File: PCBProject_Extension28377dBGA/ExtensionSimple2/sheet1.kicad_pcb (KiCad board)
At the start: 4 copper layers, 122.2 x 82.1 mm, 88 parts, among them J1 Conn_02x05_Odd_Even, J2 Conn_01x02_Pin, J3 Conn_01x02_Pin, Q1 FMMT618TA, U1 SN74ABT541, U2 SN74ABT541

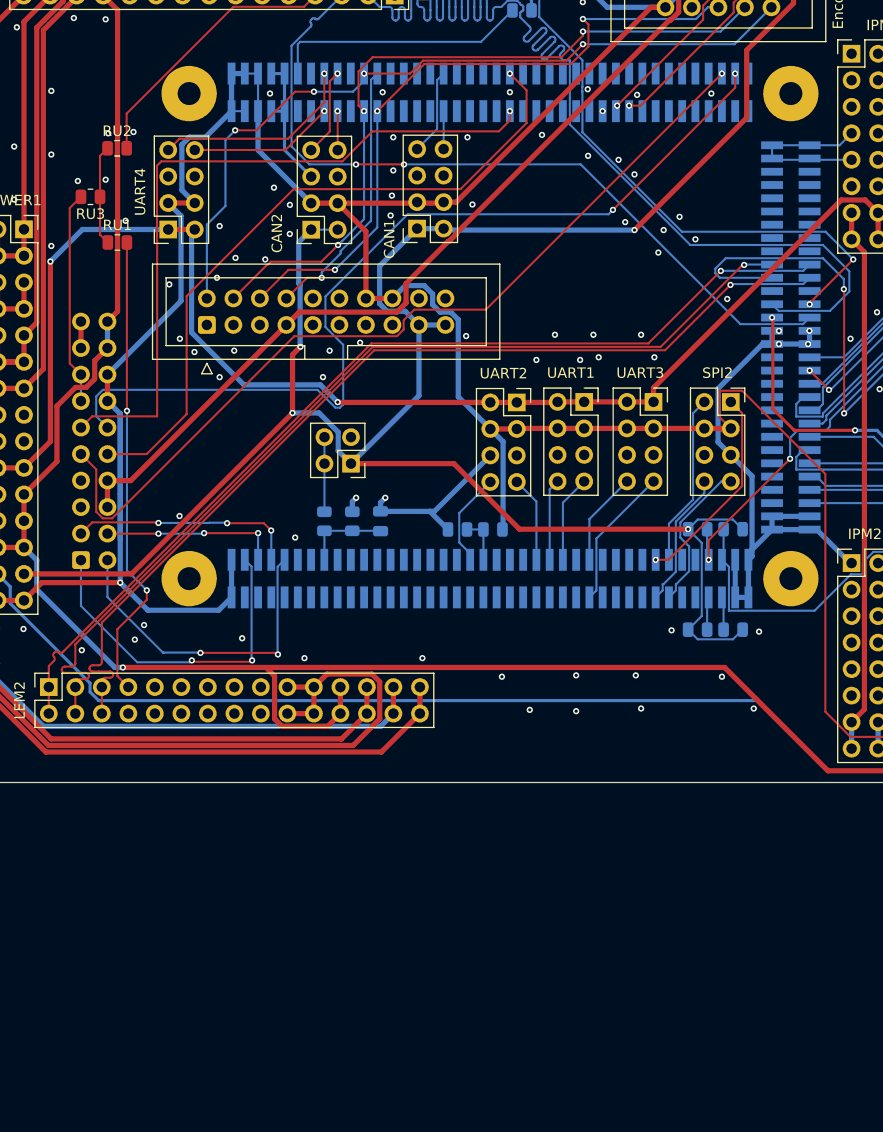
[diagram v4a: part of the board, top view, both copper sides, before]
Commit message: 底板原理图中加入RS485通讯芯片—-SN65HVD75
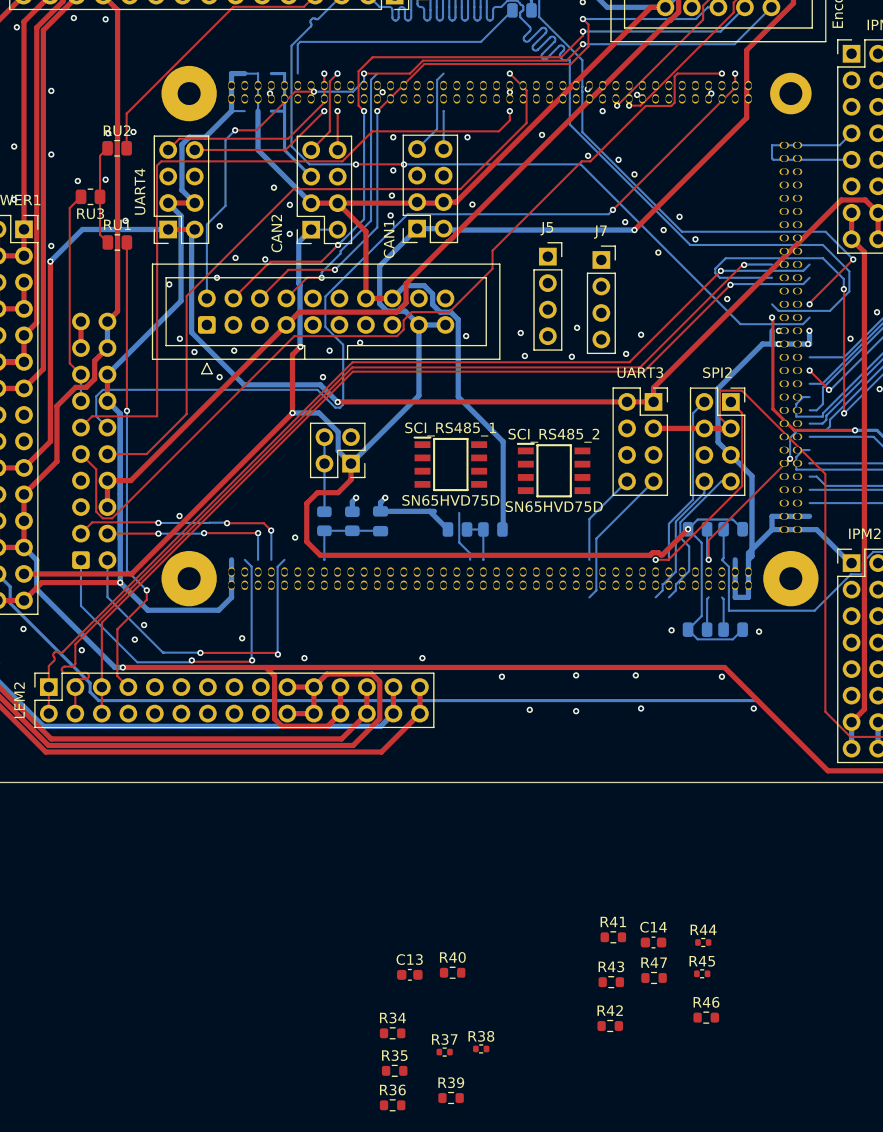
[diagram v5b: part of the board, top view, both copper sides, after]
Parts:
- removed UART1, UART2: Conn_02x04_Counter_Clockwise, Connector_PinSocket_2.54mm:PinSocket_2x04_P2.54mm_Vertical
- added C13: 0.1uF, Capacitor_SMD:C_0603_1608Metric, F.Cu at (235.3, 174.5)
- added C14: 0.1uF, Capacitor_SMD:C_0603_1608Metric, F.Cu at (258.6, 171.4)
- added J5: RS485_1_CONNECT, Connector_PinSocket_2.54mm:PinSocket_1x04_P2.54mm_Vertical, F.Cu at (248.5, 105.7)
- added J7: RS485_2_CONNECT, Connector_PinSocket_2.54mm:PinSocket_1x04_P2.54mm_Vertical, F.Cu at (253.6, 106.0)
- added R34: 10K, Resistor_SMD:R_0603_1608Metric, F.Cu at (233.6, 180.1)
- added R35: 10K, Resistor_SMD:R_0603_1608Metric, F.Cu at (233.8, 183.7)
- added R36: 120R, Resistor_SMD:R_0603_1608Metric, F.Cu at (233.6, 187.0)
- added R37: 10R, Resistor_SMD:R_0402_1005Metric, F.Cu at (238.6, 181.9)
- added R38: 10R, Resistor_SMD:R_0402_1005Metric, F.Cu at (242.1, 181.6)
- added R39: 10K, Resistor_SMD:R_0603_1608Metric, F.Cu at (239.2, 186.3)
- added R40: 10K, Resistor_SMD:R_0603_1608Metric, F.Cu at (239.4, 174.3)
- added R41: 10K, Resistor_SMD:R_0603_1608Metric, F.Cu at (254.8, 170.9)
- added R42: 10K, Resistor_SMD:R_0603_1608Metric, F.Cu at (254.5, 179.4)
- added R43: 120R, Resistor_SMD:R_0603_1608Metric, F.Cu at (254.6, 175.2)
- added R44: 10R, Resistor_SMD:R_0402_1005Metric, F.Cu at (263.4, 171.4)
- added R45: 10R, Resistor_SMD:R_0402_1005Metric, F.Cu at (263.3, 174.4)
- added R46: 10K, Resistor_SMD:R_0603_1608Metric, F.Cu at (263.7, 178.6)
- added R47: 10K, Resistor_SMD:R_0603_1608Metric, F.Cu at (258.7, 174.8)
- added SCI_RS485_1: SN65HVD75D, Oshinoko:SOIC127P600X175-8N, F.Cu at (239.2, 125.6)
- added SCI_RS485_2: SN65HVD75D, Oshinoko:SOIC127P600X175-8N, F.Cu at (249.1, 126.2)
- DSP1: footprint 1mmlab_footprint:DSP_240_SMD -> Oshinoko:DSP_240_0p6mm
- N1: footprint 1mmlab_footprint:SOIC14_M -> Oshinoko:SOIC14_M
- U1, U2: footprint 1mmlab_footprint:TSSOP-20 -> Oshinoko:TSSOP-20
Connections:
- DSP1 pad 133: unconnected-(DSP1-133_GP134-Pad133) -> /UART_WRB
- DSP1 pad 141: unconnected-(DSP1-141_GP132-Pad141) -> /UART_WRA
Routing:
- net D+5V: track 354.1 -> 338.5 mm
- net VDD: track 216.5 -> 230.3 mm
- net /UART_SCI_TXDA: track 8.35 -> 0.00 mm
- net /UART_SCI_RXDB: track 8.24 -> 0.00 mm
- net /UART_SCI_RXDA: track 7.83 -> 0.00 mm
- net AGND: track 259.8 -> 252.3 mm, vias 145 -> 144
- net /UART_SCI_TXDB: track 9.13 -> 4.92 mm
- net /IPM_IU2: track 93.9 -> 90.2 mm
- net /SPI_A_MO_HS: track 84.5 -> 87.0 mm
- net D12V1: track 179.4 -> 178.8 mm

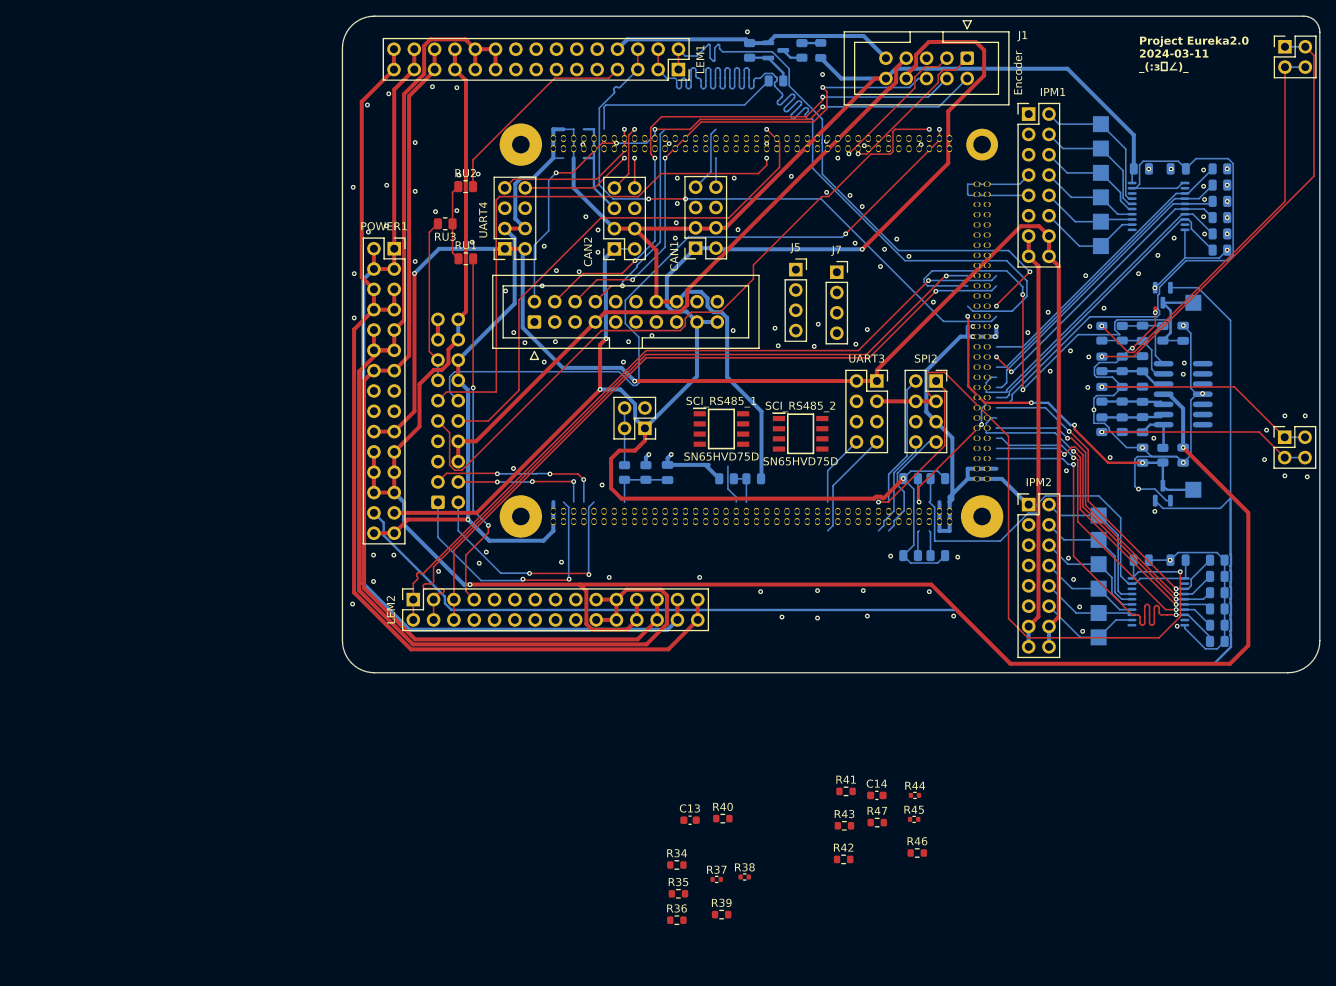
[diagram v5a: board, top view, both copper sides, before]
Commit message: 底板中增加了CAN转TTL模块，并初步修改了底板的尺寸
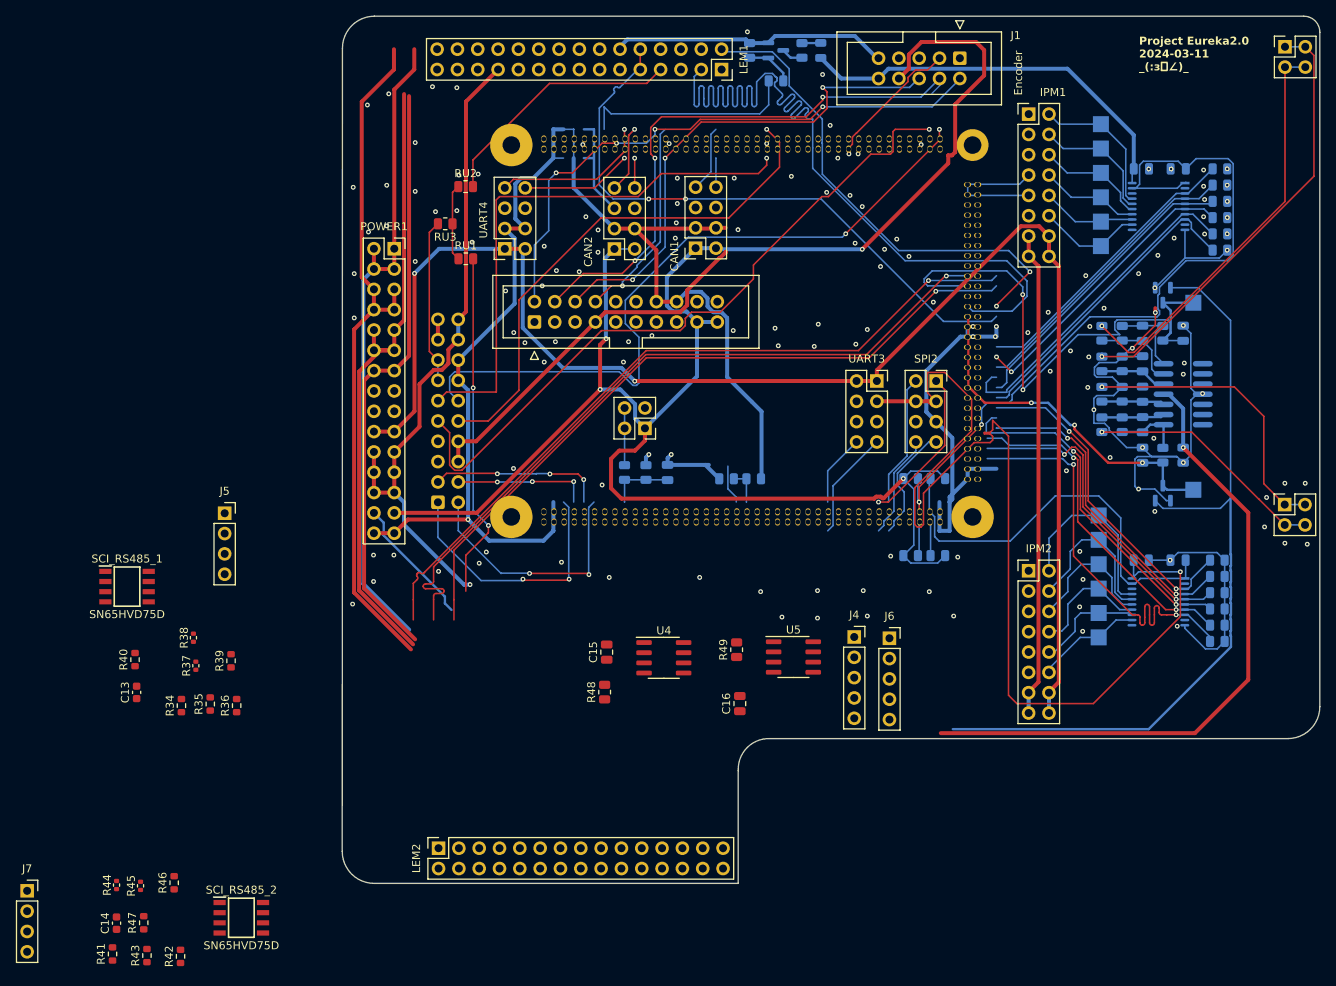
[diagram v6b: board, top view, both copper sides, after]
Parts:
- added C15: 104, Capacitor_SMD:C_0805_2012Metric, F.Cu at (224.9, 153.5)
- added C16: 104, Capacitor_SMD:C_0805_2012Metric, F.Cu at (241.5, 159.9)
- added J4: CAN_1_CONNECT, Connector_PinSocket_2.54mm:PinSocket_1x05_P2.54mm_Vertical, F.Cu at (255.8, 151.6)
- added J6: CAN_2_CONNECT, Connector_PinSocket_2.54mm:PinSocket_1x05_P2.54mm_Vertical, F.Cu at (260.2, 151.8)
- added R48: 4.7k, Resistor_SMD:R_0805_2012Metric, F.Cu at (224.6, 158.5)
- added R49: 4.7k, Resistor_SMD:R_0805_2012Metric, F.Cu at (241.1, 153.2)
- added U4: SN65HVD230, Package_SO:SOIC-8_3.9x4.9mm_P1.27mm, F.Cu at (232.0, 154.2)
- added U5: SN65HVD230, Package_SO:SOIC-8_3.9x4.9mm_P1.27mm, F.Cu at (248.2, 154.1)
- moved J7 127.4 mm to (152.4, 183.3)
- moved R44 100.4 mm to (163.6, 182.6), turned to 90 degrees
- moved R45 97.1 mm to (166.6, 182.7), turned to 90 degrees
- moved C14 96.4 mm to (163.6, 187.4), turned to 90 degrees
- moved R41 93.9 mm to (163.1, 191.2), turned to 90 degrees
- moved R46 93.0 mm to (170.8, 182.3), turned to 90 degrees
- moved R47 92.5 mm to (167.0, 187.3), turned to 90 degrees
- moved SCI_RS485_2 92.5 mm to (179.2, 186.7)
- moved R43 88.7 mm to (167.4, 191.4), turned to 90 degrees
- moved R42 83.8 mm to (171.6, 191.5), turned to 90 degrees
- moved J5 77.6 mm to (177.1, 136.1)
- moved SCI_RS485_1 76.9 mm to (164.9, 145.3)
- moved R40 76.1 mm to (165.9, 154.4), turned to 90 degrees
- moved R38 75.1 mm to (173.2, 151.7), turned to 90 degrees
- moved C13 71.0 mm to (166.1, 158.5), turned to 90 degrees
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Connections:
- C1 pad 1: AGND -> unconnected-(C1-Pad1)
- C1 pad 2: /DSP_PWM1~{_ENABL}E -> unconnected-(C1-Pad2)
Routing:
- net /IPM_IU1: track 76.4 -> 0.00 mm, vias 2 -> 0
- net A+5V: track 237.3 -> 164.0 mm
- net 12VGND: track 153.0 -> 80.0 mm
- net AGND: track 252.3 -> 318.7 mm
- net AVDD: track 177.8 -> 115.8 mm
- net A-5V: track 115.3 -> 74.4 mm
- net -12: track 126.3 -> 86.5 mm
- net +12: track 118.2 -> 81.6 mm
- net PE_GND: track 80.5 -> 46.9 mm
- net D+5V: track 338.5 -> 358.8 mm
- net /QEP1_HALL_U: track 69.6 -> 51.1 mm
- net /IPM_IW1: track 74.4 -> 61.4 mm
- net /DC_BUS_2M1: track 28.0 -> 36.4 mm
- net D12V1: track 178.8 -> 187.0 mm
- net D12VGND: track 52.4 -> 60.5 mm
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- removed copper zone on In1.Cu, net AGND
- removed copper zone on In2.Cu, net AGND
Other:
- board size 122.2 x 82.1 mm -> 122.2 x 108.4 mm
